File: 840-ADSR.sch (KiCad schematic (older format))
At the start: 97 parts, among them J1 PJ-301B-JACK, J2 PJ-301B-JACK, J3 PJ-301B-JACK, J4 PJ-301B-JACK, J5 PJ-301B, J6 PJ-301B, J7 PJ-301B, P1 CONN_02X05, Q1 MMBT3904, Q2 MMBT3904, Q3 MMBT3904, Q4 DMMT3904W, Q5 DMMT3906W-K4B, SW1 B3F-1050, T1 10K, T2 10K, U1 CD4052, U2 NE555, U3 TL074-, U4 TL072-

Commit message: footprints associated, starting placing
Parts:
- C1, C10, C11, C12, C13, C14, C15, C16, C2, C3, C4, C5, C6, C7, C8, C9: footprint MyModules:SM0603-C-JRL -> MyModules:SM0603-C-MURATA
- C17, C18: footprint Capacitors_SMD:c_elec_5x5.3 -> MyModules:jrl_c_elec_5x5.3
- C20, C21, C22, C23: footprint (none) -> MyModules:SM0603-C-MURATA
- C24: footprint ~ -> MyModules:SM0603-C-MURATA
- D4: footprint ~ -> MyModules:SOT23-132-JRL
- D5: footprint (none) -> MyModules:SOD323-C1A2
- D6: footprint (none) -> MyModules:3MM-LED-C1A2
- F1, F2: footprint Capacitors_SMD:C_0805 -> MyModules:SM0805-HAND
- P1: footprint Pin_Headers:Pin_Header_Straight_2x05 -> Pin_Headers:Pin_Header_Straight_2x05_Pitch2.54mm
- Q3: footprint SOT-23 -> MyModules:SOT23-132-JRL
- R1, R2, R3, R4, R5, R6, R7, R8, R9: footprint MyModules:SM0603-R-JRL -> MyModules:SM0603-R-YAGEO
- R10, R11, R12, R13, R14, R15, R16, R17, R18, R19, R20, R21, R22, R23, R24, R25, R26, R27, R28, R29, R30, R31, R32, R33, R34: footprint (none) -> MyModules:SM0603-R-YAGEO
- R35, R36, R37, R38, R39, R40: footprint ~ -> MyModules:SM0603-R-YAGEO
- T1, T2: footprint ~ -> MyModules:TC33X-2
- U1: footprint (none) -> MyModules:TSSOP-16_4.4x5mm_Pitch0.65mm_jrl
- U2, U4: footprint ~ -> MyModules:TSSOP-8_4.4x3mm_Pitch0.65mm
- U3: footprint (none) -> Housings_SSOP:TSSOP-14_4.4x5mm_Pitch0.65mm

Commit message: parts mostly placed, starting to route
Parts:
- removed C10, C11, C12, C13, C14, C15, C16, C8, C9: 0.1µ, MyModules:SM0603-C-MURATA, symbol C_US

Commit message: almost done routing
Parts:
- removed R1, R2, R3, R4: 10K, MyModules:SM0603-R-YAGEO, symbol R_US
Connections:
- net +10V: now also J1.2, J2.2, J3.2, J4.2
- net +12V: now also U3.4 (V+); no longer U3.4 (V+)
- net -12V: now also U3.11 (V-); no longer U3.11 (V-)
- net GND: now also Q5.1 (B), U3.3 (+); no longer Q5.2 (B), U3.10 (+)
- net at R32.2, R33.1: now also U3.8; no longer U3.1
- net at R25.2, R32.1: now also U3.9 (-); no longer U3.2 (-)
- net at R26.2, R29.2: now also U3.10 (+); no longer U3.3 (+)
- net at C22.1, R24.1: now also U3.1; no longer U3.8
- net at C22.2, Q4.6 (C), R23.1: now also Q5.6 (C), U3.2 (-); no longer Q5.3 (C), U3.9 (-)
- net at C23.2, Q4.3 (C), U3.6 (-): now also Q5.3 (C); no longer Q5.6 (C)
- net at R19.2, R20.2, T1.2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: now also Q5.2 (B); no longer Q5.1 (B)
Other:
- moved on the sheet: C22, Q5A, Q5B

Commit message: routed, need to place silk screen labels
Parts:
- removed C2: 0.1µ, MyModules:SM0603-C-MURATA, symbol C_US
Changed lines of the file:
@@
 	7125 4725 7275 4725
 Wire Wire Line
-	7275 4725 7275 3525
-Wire Wire Line
-	7275 3525 4375 3525
+	7275 3525 7275 4725
+Wire Wire Line
+	4375 3525 7275 3525
 Wire Wire Line
 	4375 3525 4375 3575
@@
 $EndComp
 $Comp
-L C_US C2
-U 1 1 5B2C1077
-P 1850 13800
-F 0 "C2" H 1900 13900 50  0000 L CNN
-F 1 "0.1µ" H 1900 13700 50  0000 L CNN
-F 2 "MyModules:SM0603-C-MURATA" H 1850 13800 60  0001 C CNN
-F 3 "~" H 1850 13800 60  0000 C CNN
-	1    1850 13800
-	1    0    0    -1
-$EndComp
-$Comp
 L C_US C4
 U 1 1 5B2C107E
@@
 	1    2250 13800
 	1    0    0    -1
-$EndComp
-$Comp
-L -12V #PWR039
-U 1 1 5B2C1085
-P 1850 14000
-F 0 "#PWR039" H 1850 14100 30  0001 C CNN
-F 1 "-12V" H 1825 14275 60  0000 C CNN
-F 2 "~" H 1850 14000 60  0000 C CNN
-F 3 "~" H 1850 14000 60  0000 C CNN
-	1    1850 14000
-	-1   0    0    1
 $EndComp
 $Comp
@@
 $EndComp
 $Comp
-L GND_E #PWR040
+L GND_E #PWR039
 U 1 1 5B2C109E
 P 7450 13400
-F 0 "#PWR040" V 7450 13400 30  0001 C CNN
+F 0 "#PWR039" V 7450 13400 30  0001 C CNN
 F 1 "GND_E" H 7450 13330 30  0001 C CNN
 F 2 "" H 7450 13400 60  0000 C CNN
@@
 $EndComp
 $Comp
-L GND_E #PWR041
+L GND_E #PWR040
 U 1 1 5B2C10A4
 P 6300 13275
-F 0 "#PWR041" V 6300 13275 30  0001 C CNN
+F 0 "#PWR040" V 6300 13275 30  0001 C CNN
 F 1 "GND_E" H 6300 13205 30  0001 C CNN
 F 2 "" H 6300 13275 60  0000 C CNN
@@
 $EndComp
 $Comp
-L +12V #PWR042
+L +12V #PWR041
 U 1 1 5B2C10AA
 P 5800 12400
-F 0 "#PWR042" H 5800 12250 50  0001 C CNN
+F 0 "#PWR041" H 5800 12250 50  0001 C CNN
 F 1 "+12V" H 5800 12540 50  0000 C CNN
 F 2 "" H 5800 12400 60  0000 C CNN
@@
 $EndComp
 $Comp
-L -12V #PWR043
+L -12V #PWR042
 U 1 1 5B2C10BE
 P 5800 13700
-F 0 "#PWR043" H 5800 13550 50  0001 C CNN
+F 0 "#PWR042" H 5800 13550 50  0001 C CNN
 F 1 "-12V" H 5800 13840 50  0000 C CNN
 F 2 "" H 5800 13700 60  0000 C CNN
@@
 $EndComp
 $Comp
-L GND_E #PWR044
+L GND_E #PWR043
 U 1 1 5B2C10D9
 P 6650 11900
-F 0 "#PWR044" V 6650 11900 30  0001 C CNN
+F 0 "#PWR043" V 6650 11900 30  0001 C CNN
 F 1 "GND_E" H 6650 11830 30  0001 C CNN
 F 2 "" H 6650 11900 60  0000 C CNN
@@
 Connection ~ 2250 13100
 Wire Wire Line
-	1850 12600 1850 13600
-Connection ~ 1850 13100
+	1850 12600 1850 13100
 Wire Wire Line
 	6750 12950 6750 13150
@@
 $EndComp
 $Comp
-L PWR #FLG045
+L PWR #FLG044
 U 1 1 5B2C1128
 P 5450 12425
-F 0 "#FLG045" H 5450 12520 30  0001 C CNN
+F 0 "#FLG044" H 5450 12520 30  0001 C CNN
 F 1 "PWR" H 5450 12605 30  0000 C CNN
 F 2 "" H 5450 12425 60  0000 C CNN
@@
 Connection ~ 5450 12600
 $Comp
-L PWR #FLG046
+L PWR #FLG045
 U 1 1 5B2C112F
 P 5450 13700
-F 0 "#FLG046" H 5450 13795 30  0001 C CNN
+F 0 "#FLG045" H 5450 13795 30  0001 C CNN
 F 1 "PWR" H 5450 13880 30  0000 C CNN
 F 2 "" H 5450 13700 60  0000 C CNN
@@
 Connection ~ 5450 13500
 $Comp
-L PWR #FLG047
+L PWR #FLG046
 U 1 1 5B2C1136
 P 5050 13075
-F 0 "#FLG047" H 5050 13170 30  0001 C CNN
+F 0 "#FLG046" H 5050 13170 30  0001 C CNN
 F 1 "PWR" H 5050 13255 30  0000 C CNN
 F 2 "" H 5050 13075 60  0000 C CNN
@@
 $EndComp
 $Comp
-L GND_E #PWR048
+L GND_E #PWR047
 U 1 1 5B2CC6A0
 P 12300 12825
-F 0 "#PWR048" V 12300 12825 30  0001 C CNN
+F 0 "#PWR047" V 12300 12825 30  0001 C CNN
 F 1 "GND_E" H 12300 12755 30  0001 C CNN
 F 2 "" H 12300 12825 60  0000 C CNN
@@
 $EndComp
 $Comp
-L +12V #PWR049
+L +12V #PWR048
 U 1 1 5B2CC6C8
 P 13225 11775
-F 0 "#PWR049" H 13225 11625 50  0001 C CNN
+F 0 "#PWR048" H 13225 11625 50  0001 C CNN
 F 1 "+12V" H 13225 11915 50  0000 C CNN
 F 2 "" H 13225 11775 60  0000 C CNN
@@
 $EndComp
 $Comp
-L +12V #PWR050
+L +12V #PWR049
 U 1 1 5B2CC6F9
 P 14300 12625
-F 0 "#PWR050" H 14300 12475 50  0001 C CNN
+F 0 "#PWR049" H 14300 12475 50  0001 C CNN
 F 1 "+12V" H 14300 12765 50  0000 C CNN
 F 2 "" H 14300 12625 60  0000 C CNN
@@
 $EndComp
 $Comp
-L GND_E #PWR051
+L GND_E #PWR050
 U 1 1 5B2CC70D
 P 14300 13900
-F 0 "#PWR051" V 14300 13900 30  0001 C CNN
+F 0 "#PWR050" V 14300 13900 30  0001 C CNN
 F 1 "GND_E" H 14300 13830 30  0001 C CNN
 F 2 "" H 14300 13900 60  0000 C CNN
@@
 	12300 12375 12525 12375
 $Comp
-L +12V #PWR052
+L +12V #PWR051
 U 1 1 5B2D144D
 P 12050 13175
-F 0 "#PWR052" H 12050 13025 50  0001 C CNN
+F 0 "#PWR051" H 12050 13025 50  0001 C CNN
 F 1 "+12V" H 12050 13315 50  0000 C CNN
 F 2 "" H 12050 13175 60  0000 C CNN
@@
 GATE
 $Comp
-L GND_E #PWR053
+L GND_E #PWR052
 U 1 1 5B2D609E
 P 12800 14575
-F 0 "#PWR053" V 12800 14575 30  0001 C CNN
+F 0 "#PWR052" V 12800 14575 30  0001 C CNN
 F 1 "GND_E" H 12800 14505 30  0001 C CNN
 F 2 "" H 12800 14575 60  0000 C CNN
@@
 Connection ~ 13450 6075
 $Comp
-L GND_E #PWR054
+L GND_E #PWR053
 U 1 1 5B2C7250
 P 13850 6925
-F 0 "#PWR054" V 13850 6925 30  0001 C CNN
+F 0 "#PWR053" V 13850 6925 30  0001 C CNN
 F 1 "GND_E" H 13850 6855 30  0001 C CNN
 F 2 "~" H 13850 6925 60  0000 C CNN
@@
 	12925 4325 13625 4325
 $Comp
-L GND_E #PWR055
+L GND_E #PWR054
 U 1 1 5B2C7B56
 P 13625 4750
-F 0 "#PWR055" V 13625 4750 30  0001 C CNN
+F 0 "#PWR054" V 13625 4750 30  0001 C CNN
 F 1 "GND_E" H 13625 4680 30  0001 C CNN
 F 2 "~" H 13625 4750 60  0000 C CNN
@@
 $EndComp
 $Comp
-L +10V #PWR056
+L +10V #PWR055
 U 1 1 5B297D32
 P 10125 11825
-F 0 "#PWR056" H 10125 11675 50  0001 C CNN
+F 0 "#PWR055" H 10125 11675 50  0001 C CNN
 F 1 "+10V" H 10125 11965 50  0000 C CNN
 F 2 "" H 10125 11825 60  0000 C CNN
@@
 $EndComp
 $Comp
-L GND_E #PWR057
+L GND_E #PWR056
 U 1 1 5B298E15
 P 9525 11925
-F 0 "#PWR057" V 9525 11925 30  0001 C CNN
+F 0 "#PWR056" V 9525 11925 30  0001 C CNN
 F 1 "GND_E" H 9525 11855 30  0001 C CNN
 F 2 "~" H 9525 11925 60  0000 C CNN
@@
 $EndComp
 $Comp
-L GND_E #PWR058
+L GND_E #PWR057
 U 1 1 5B2991CC
 P 10375 12000
-F 0 "#PWR058" V 10375 12000 30  0001 C CNN
+F 0 "#PWR057" V 10375 12000 30  0001 C CNN
 F 1 "GND_E" H 10375 11930 30  0001 C CNN
 F 2 "~" H 10375 12000 60  0000 C CNN
@@
 $EndComp
 $Comp
-L +10V #PWR059
+L +10V #PWR058
 U 1 1 5B29E720
 P 10150 12650
-F 0 "#PWR059" H 10150 12500 50  0001 C CNN
+F 0 "#PWR058" H 10150 12500 50  0001 C CNN
 F 1 "+10V" H 10150 12790 50  0000 C CNN
 F 2 "" H 10150 12650 60  0000 C CNN
@@
 $EndComp
 $Comp
-L GND_E #PWR060
+L GND_E #PWR059
 U 1 1 5B29E732
 P 9550 12750
-F 0 "#PWR060" V 9550 12750 30  0001 C CNN
+F 0 "#PWR059" V 9550 12750 30  0001 C CNN
 F 1 "GND_E" H 9550 12680 30  0001 C CNN
 F 2 "~" H 9550 12750 60  0000 C CNN
@@
 $EndComp
 $Comp
-L GND_E #PWR061
+L GND_E #PWR060
 U 1 1 5B29E738
 P 10400 12825
-F 0 "#PWR061" V 10400 12825 30  0001 C CNN
+F 0 "#PWR060" V 10400 12825 30  0001 C CNN
 F 1 "GND_E" H 10400 12755 30  0001 C CNN
 F 2 "~" H 10400 12825 60  0000 C CNN
@@
 $EndComp
 $Comp
-L +10V #PWR062
+L +10V #PWR061
 U 1 1 5B29EADE
 P 10150 13600
-F 0 "#PWR062" H 10150 13450 50  0001 C CNN
+F 0 "#PWR061" H 10150 13450 50  0001 C CNN
 F 1 "+10V" H 10150 13740 50  0000 C CNN
 F 2 "" H 10150 13600 60  0000 C CNN
@@
 $EndComp
 $Comp
-L GND_E #PWR063
+L GND_E #PWR062
 U 1 1 5B29EAF0
 P 9550 13700
-F 0 "#PWR063" V 9550 13700 30  0001 C CNN
+F 0 "#PWR062" V 9550 13700 30  0001 C CNN
 F 1 "GND_E" H 9550 13630 30  0001 C CNN
 F 2 "~" H 9550 13700 60  0000 C CNN
@@
 $EndComp
 $Comp
-L GND_E #PWR064
+L GND_E #PWR063
 U 1 1 5B29EAF6
 P 10400 13775
-F 0 "#PWR064" V 10400 13775 30  0001 C CNN
+F 0 "#PWR063" V 10400 13775 30  0001 C CNN
 F 1 "GND_E" H 10400 13705 30  0001 C CNN
 F 2 "~" H 10400 13775 60  0000 C CNN
@@
 	10150 13600 10150 13775
 Wire Wire Line
-	9900 13775 10150 13775
-Wire Wire Line
-	9900 13300 9900 13775
+	10150 13775 9900 13775
+Wire Wire Line
+	9900 13775 9900 13300
 $Comp
 L POT_US VR4
@@
 $EndComp
 $Comp
-L +10V #PWR065
+L +10V #PWR064
 U 1 1 5B29EB0D
 P 10175 14425
-F 0 "#PWR065" H 10175 14275 50  0001 C CNN
+F 0 "#PWR064" H 10175 14275 50  0001 C CNN
 F 1 "+10V" H 10175 14565 50  0000 C CNN
 F 2 "" H 10175 14425 60  0000 C CNN
@@
 $EndComp
 $Comp
-L GND_E #PWR066
+L GND_E #PWR065
 U 1 1 5B29EB1F
 P 9575 14525
-F 0 "#PWR066" V 9575 14525 30  0001 C CNN
+F 0 "#PWR065" V 9575 14525 30  0001 C CNN
 F 1 "GND_E" H 9575 14455 30  0001 C CNN
 F 2 "~" H 9575 14525 60  0000 C CNN
@@
 $EndComp
 $Comp
-L GND_E #PWR067
+L GND_E #PWR066
 U 1 1 5B29EB25
 P 10425 14600
-F 0 "#PWR067" V 10425 14600 30  0001 C CNN
+F 0 "#PWR066" V 10425 14600 30  0001 C CNN
 F 1 "GND_E" H 10425 14530 30  0001 C CNN
 F 2 "~" H 10425 14600 60  0000 C CNN
@@
 INV OUT
 $Comp
-L PWR #FLG068
+L PWR #FLG067
 U 1 1 5B2D84C1
 P 15900 3075
-F 0 "#FLG068" H 15900 3170 30  0001 C CNN
+F 0 "#FLG067" H 15900 3170 30  0001 C CNN
 F 1 "PWR" H 15900 3255 30  0000 C CNN
 F 2 "" H 15900 3075 60  0000 C CNN
@@
 	1850 13100 3050 13100
 $Comp
-L GND_E #PWR069
+L GND_E #PWR068
 U 1 1 5B339927
 P 3050 13600
-F 0 "#PWR069" V 3050 13600 30  0001 C CNN
+F 0 "#PWR068" V 3050 13600 30  0001 C CNN
 F 1 "GND_E" H 3050 13530 30  0001 C CNN
 F 2 "" H 3050 13600 60  0000 C CNN

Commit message: added .gitignore and some silk screen tweaking
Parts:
- renumbered C21 to C10, C3 to C11, C19 to C12, C6 to C13, C7 to C14, C17 to C2, C18 to C3, C24 to C4, C4 to C5, C5 to C6, C20 to C7, C23 to C8, C22 to C9, D4 to D3, D5 to D4, D6 to D5, D3 to D6, J7 to J5, J5 to J7, Q5 to Q1, Q4 to Q2, Q1 to Q4, Q2 to Q5, R35 to R1, R23 to R10, R15 to R11, R16 to R12, R24 to R13, R17 to R14, R10 to R15, R14 to R16, R19 to R17, R20 to R18, R22 to R19, R28 to R2, R21 to R20, R18 to R21, R37 to R22, R36 to R23, R38 to R24, R39 to R25, R13 to R26, R7 to R27, R34 to R28, R12 to R29, R31 to R3, R33 to R30, R5 to R31, R8 to R32, R11 to R33, R6 to R34, R9 to R35, R40 to R36, R29 to R4, R27 to R5, R26 to R6, R32 to R7, R25 to R8, R30 to R9, U3 to U1, U1 to U3

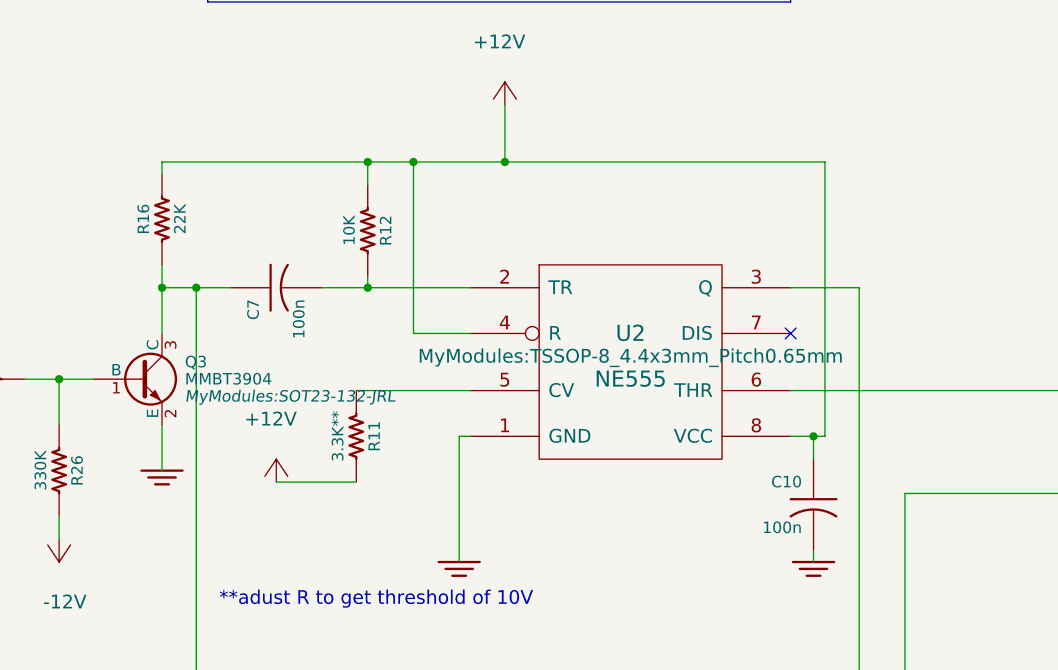
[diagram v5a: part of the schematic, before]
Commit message: delted 3.3K resistor connected to 555 CV pin and replaced wtih 10V reference. duh.
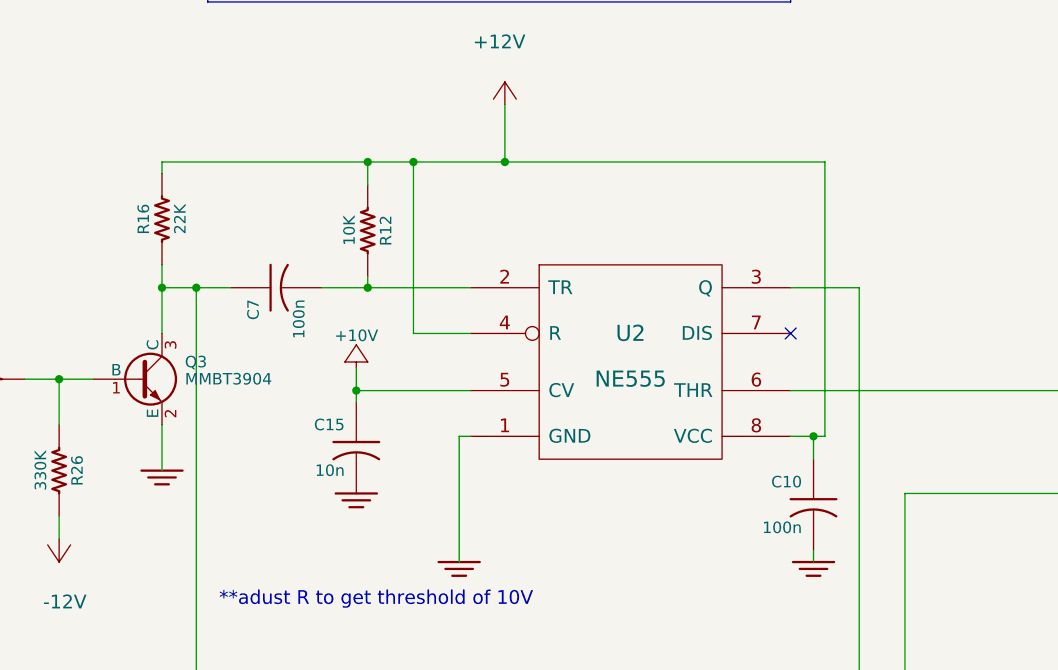
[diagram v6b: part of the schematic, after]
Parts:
- removed R11: 3.3K**, MyModules:SM0603-R-YAGEO, symbol R_US
- added C15: 10n, MyModules:SM0603-C-MURATA, symbol C_US
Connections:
- net +10V: now also U2.5 (CV), C15.1
- net GND: now also C15.2

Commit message: prototype built, needs tweaking, about to start
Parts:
- R1: value 1K -> 220
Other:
- note added: "*ADJUST R7/R8 with T1/T2 \n to get 20-25 s max A/D/R\n"
- note added: "A B\n0 0 Decay/Sustain\n0 1 Release\n1 0 Attack\n1 1 Release\n"
- note added: "DECAY/RELEASE TRIM\nNECESSARY?"
- note added: "buffer this?"
- note added: "use 10V reference here?"
- note removed: "**adust R to get threshold of 10V"
- note removed: "*\nADJUST R7/R8 with T1/T2 \nto get 20-25 s max A/D/R\n"
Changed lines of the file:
@@
 	1    0    0    -1
 $EndComp
-Text Notes 4625 5475 0    60   ~ 0
-**adust R to get threshold of 10V
-Text Notes 5325 6275 0    60   ~ 0
-*\nADJUST R7/R8 with T1/T2 \nto get 20-25 s max A/D/R\n
+Text Notes 5500 5725 0    60   ~ 0
+*ADJUST R7/R8 with T1/T2 \n to get 20-25 s max A/D/R\n
 $Comp
 L C_US C10
@@
 P 15100 2700
 F 0 "R1" V 15180 2700 50  0000 C CNN
-F 1 "1K" V 15020 2700 50  0000 C CNN
+F 1 "220" V 15020 2700 50  0000 C CNN
 F 2 "MyModules:SM0603-R-YAGEO" H 15850 2850 60  0000 C CNN
 F 3 "~" H 15100 2700 60  0000 C CNN
@@
 	-1   0    0    -1
 $EndComp
+Text Notes 5700 6800 0    60   ~ 0
+A B\n0 0 Decay/Sustain\n0 1 Release\n1 0 Attack\n1 1 Release\n
+Text Notes 5625 7675 0    60   ~ 0
+DECAY/RELEASE TRIM\nNECESSARY?
+Text Notes 10100 4175 0    60   ~ 0
+use 10V reference here?
+Text Notes 15350 3700 0    60   ~ 0
+buffer this?
 $EndSCHEMATC

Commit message: v1.1 in the works. buffered env output to 555 threshold input, changed 10V reference distribution added some notes
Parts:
- added R11: 47K, MyModules:SM0603-R-YAGEO, symbol R_US
- added U5: TL072-, MyModules:TSSOP-8_4.4x3mm_Pitch0.65mm, symbol TL072-
- C8: value 100n** -> 100n
- R4: value 10K -> 22K
- R6: value 10K -> 1meg
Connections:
- net +10V: now also R15.1, U5.3 (+); no longer J1.2, J2.2, J3.2, J4.2
- net +12V: now also U5.8 (V+); no longer R15.1, R6.1
- net -12V: now also U5.4 (V-)
- net GND: now also J7.2, R6.2, U1.10 (+), R11.2; no longer R4.1
- net at C8.1, R28.1, R8.1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: now also U5.5 (+); no longer U2.6 (THR)
- net at R31.1, SW1.2: now also R11.1
- new net: R4.1, U2.6 (THR), U5.7
- new net: R4.2, R6.1, U5.6 (-)
- new net POT_REF: J1.2, J2.2, J3.2, J4.2, U5.1, U5.2 (-)
- no-connect marks 5 -> 4
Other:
- note added: "ADJUST FOR ATTACK\nASYMPTOPE LEVEL"
- note added: "PULL DOWN\n"
- note added: "USE 10V REFERENCE \nHERE?"
- note removed: "**match C5 value between\n ADSR modules. 95nF gives\nmin attack of <1.5ms"
- note removed: "buffer CV inputs???"
- note removed: "buffer this?"
- note removed: "use 10V reference here?"
- moved on the sheet: C9, R13
